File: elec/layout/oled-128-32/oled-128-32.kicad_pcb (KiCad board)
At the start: 2 copper layers, 1.5 x 10.5 mm, 14 parts

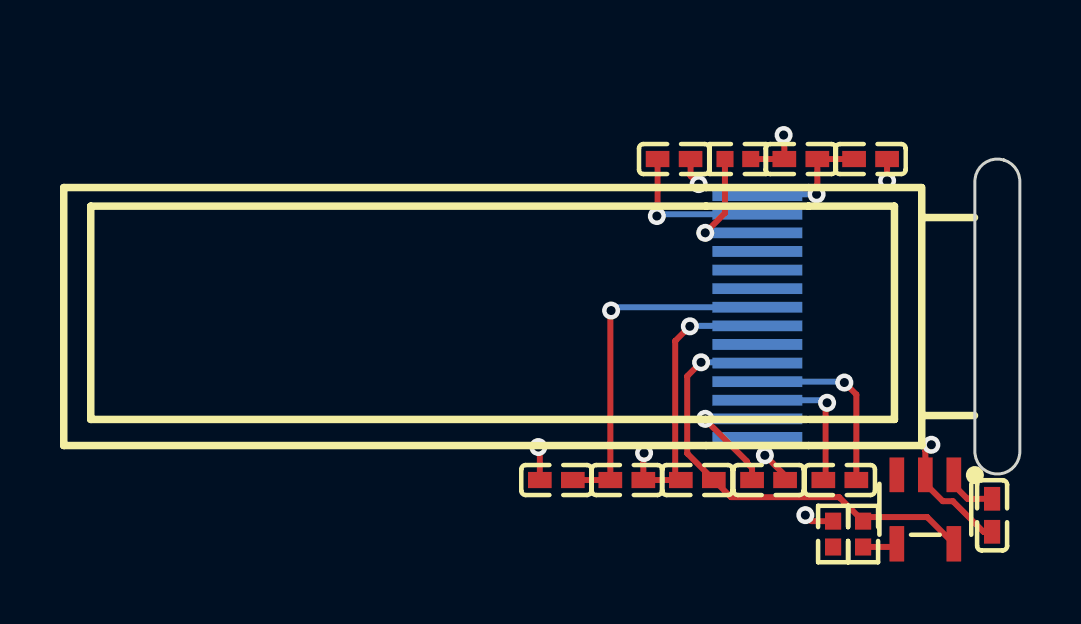
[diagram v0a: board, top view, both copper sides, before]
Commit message: cleanup CM5 pinout
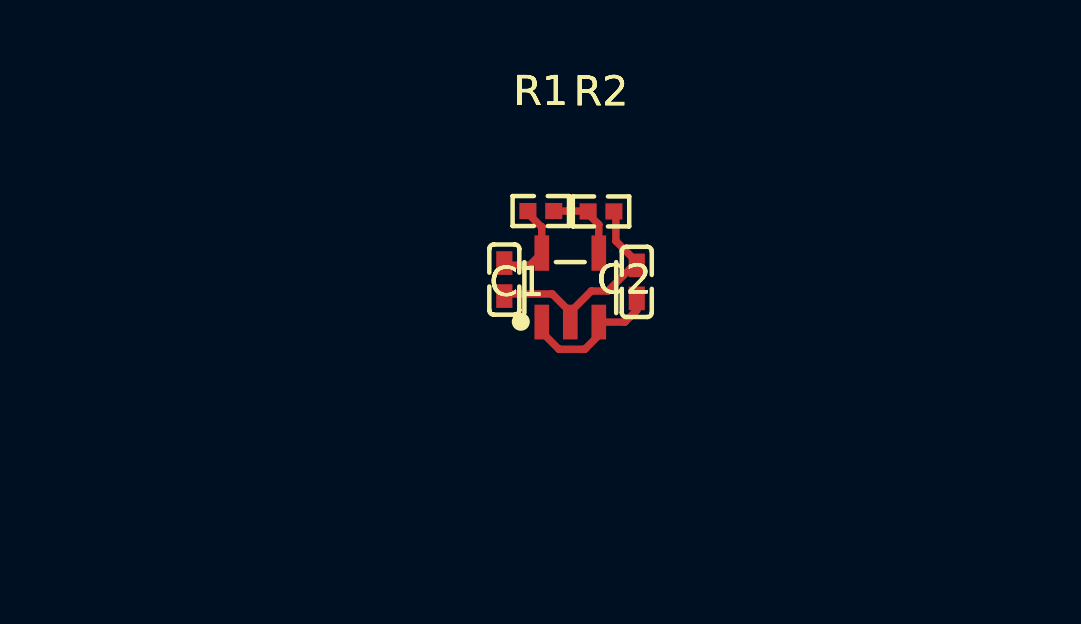
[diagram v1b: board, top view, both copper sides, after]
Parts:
- removed C3, C4: 1µF ±10% 25V X5R, atopile:C0402-b3ef17
- removed C5, C7, C8, C9: 100nF ±10% 16V X7R, atopile:C0402-b3ef17
- removed C6: 4.7µF ±20% 6.3V X5R, atopile:C0402-b3ef17
- removed OLED1: , atopile:OLED-SMD_N087-2832TSWYG02-H14_1-7d3a70
- removed R3: 10kΩ ±1% 62.5mW, atopile:R0402-56259e
- R1: value 510kΩ ±1% 62.5mW -> 18kΩ ±1% 62.5mW
- R2: value 3.9kΩ ±1% 62.5mW -> 10kΩ ±1% 62.5mW
- moved U1 14.0 mm to (148.6, 111.8), turned to 0 degrees
- moved R2 13.2 mm to (149.6, 109.2), turned to 0 degrees
- moved C2 11.1 mm to (146.4, 111.5), turned to -90 degrees
- moved C1 9.46 mm to (150.8, 111.6), turned to 90 degrees
- moved R1 6.79 mm to (147.6, 109.2)
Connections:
- C1 pad 1: C1N -> IN
- C1 pad 2: C1P -> gnd
- C2 pad 1: C2N -> OUT
- C2 pad 2: C2P -> gnd
- R1 pad 1: IREF -> OUT
- R1 pad 2: gnd -> ADJ_NC
- U1 pad 1: hv-1 -> IN
- U1 pad 3: hv-1 -> IN
- U1 pad 5: hv-3 -> OUT
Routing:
- net hv-3: track 15.4 -> 0.00 mm, vias 1 -> 0
- net gnd: track 19.8 -> 7.73 mm, vias 8 -> 0
- net hv-2: track 11.8 -> 0.00 mm, vias 1 -> 0
- net C1N: track 6.33 -> 0.00 mm, vias 1 -> 0
- net VCOMH: track 5.29 -> 0.00 mm, vias 1 -> 0
- net IN: track 0.00 -> 5.00 mm
- net C1P: track 4.99 -> 0.00 mm, vias 1 -> 0
- net IREF: track 4.47 -> 0.00 mm, vias 1 -> 0
- net C2N: track 4.42 -> 0.00 mm, vias 1 -> 0
- net hv: track 4.40 -> 0.00 mm, vias 1 -> 0
- net OUT: track 0.00 -> 3.05 mm
- net hv-1: track 1.81 -> 0.00 mm
- net C2P: track 1.80 -> 0.00 mm, vias 1 -> 0
- net ADJ_NC: track 1.17 -> 2.56 mm
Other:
- board outline removed

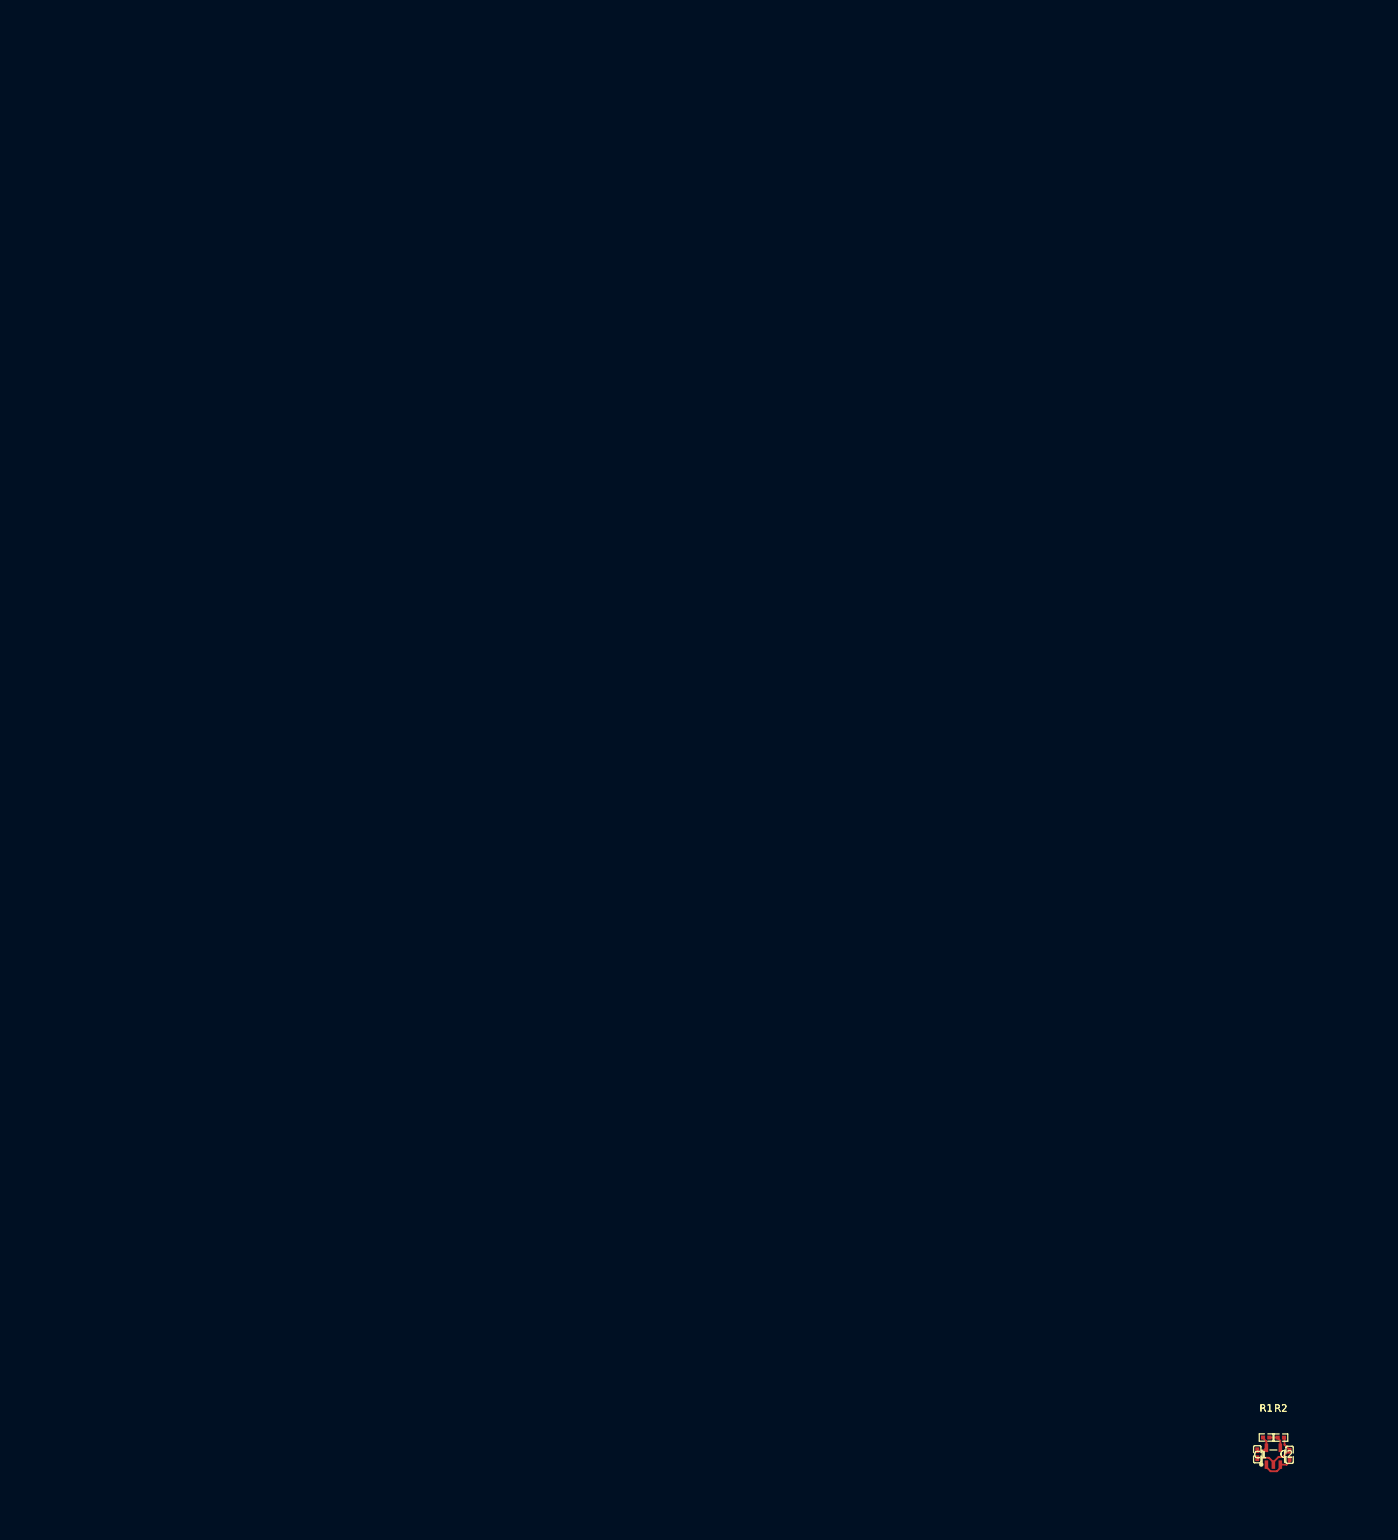
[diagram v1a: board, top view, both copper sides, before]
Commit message: update layouts to kicad 9
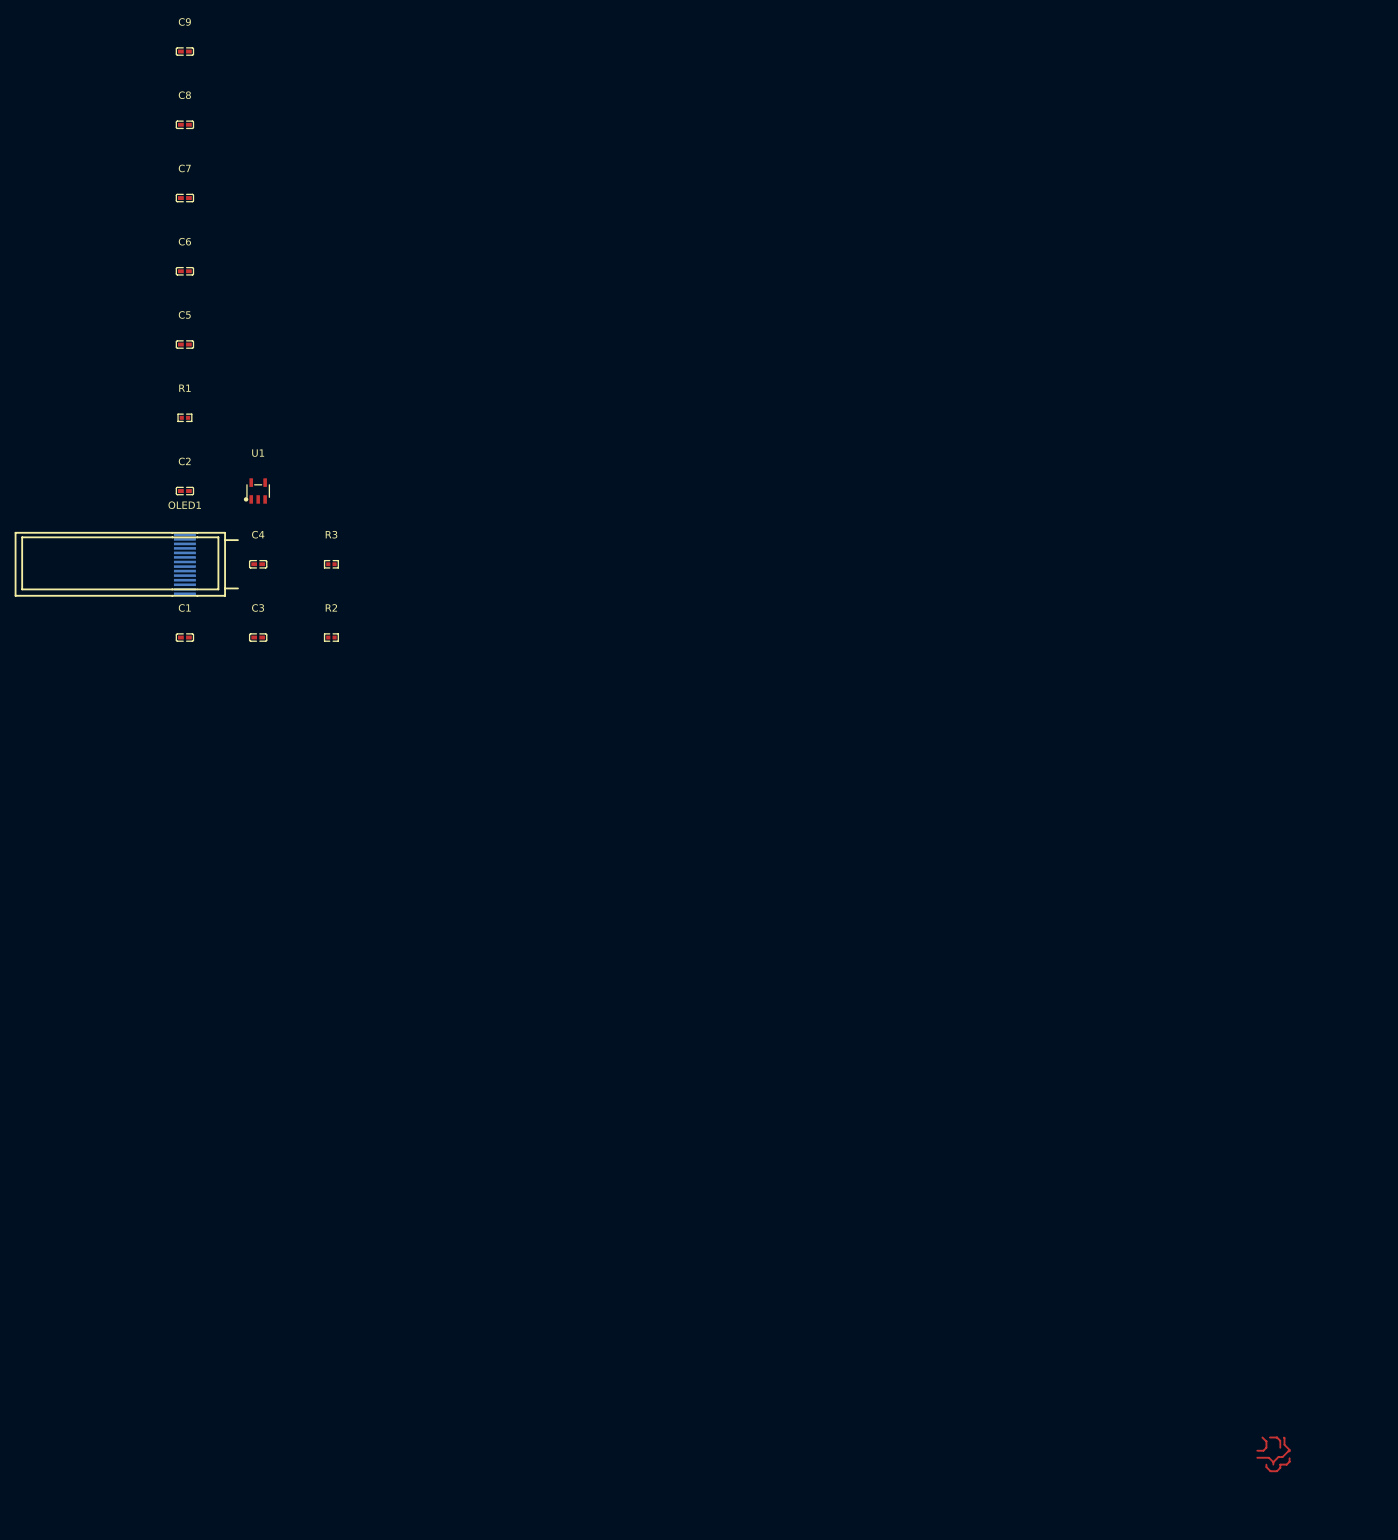
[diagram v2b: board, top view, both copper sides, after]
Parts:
- added C3: 1µF ±10% 25V X5R, atopile:C0402-b3ef17, F.Cu at (10.0, 0.00)
- added C4: 1µF ±10% 25V X5R, atopile:C0402-b3ef17, F.Cu at (10.0, -10.0)
- added C5: 100nF ±10% 16V X7R, atopile:C0402-b3ef17, F.Cu at (0.00, -40.0)
- added C6: 4.7µF ±20% 6.3V X5R, atopile:C0402-b3ef17, F.Cu at (0.00, -50.0)
- added C7: 100nF ±10% 16V X7R, atopile:C0402-b3ef17, F.Cu at (0.00, -60.0)
- added C8: 100nF ±10% 16V X7R, atopile:C0402-b3ef17, F.Cu at (0.00, -70.0)
- added C9: 100nF ±10% 16V X7R, atopile:C0402-b3ef17, F.Cu at (0.00, -80.0)
- added OLED1: , atopile:OLED-SMD_N087-2832TSWYG02-H14_1-7d3a70, F.Cu at (0.00, -10.0)
- added R3: 10kΩ ±1% 62.5mW, atopile:R0402-56259e, F.Cu at (20.0, -10.0)
- R1: value 18kΩ ±1% 62.5mW -> 510kΩ ±1% 62.5mW
- R2: value 10kΩ ±1% 62.5mW -> 3.9kΩ ±1% 62.5mW
- moved R1 202.9 mm to (0.00, -30.0)
- moved C2 196.8 mm to (0.00, -20.0), turned to 0 degrees
- moved U1 191.2 mm to (10.0, -20.0)
- moved C1 187.6 mm to (0.00, 0.00), turned to 0 degrees
- moved R2 169.5 mm to (20.0, 0.00)
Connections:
- C1 pad 1: IN -> C1N
- C1 pad 2: gnd -> C1P
- C2 pad 1: OUT -> C2N
- C2 pad 2: gnd -> C2P
- R1 pad 1: OUT -> IREF
- R1 pad 2: ADJ_NC -> gnd
- U1 pad 1: IN -> hv-1
- U1 pad 3: IN -> hv-1
- U1 pad 5: OUT -> hv
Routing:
- net (no net): track 0.00 -> 18.3 mm
- net gnd: track 7.73 -> 0.00 mm
- net IN: track 5.00 -> 0.00 mm
- net OUT: track 3.05 -> 0.00 mm
- net ADJ_NC: track 2.56 -> 0.00 mm

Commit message: building frozen
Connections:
- net line renamed SCL
- net line-1 renamed SDA
- C4 pad 1: hv -> hv-2
- C5 pad 1: hv-2 -> hv-3
- C6 pad 1: hv-2 -> hv-3
- C8 pad 1: hv-3 -> hv
- C9 pad 1: hv-3 -> hv
- OLED1 pad 14: hv-2 -> hv-3
- OLED1 pad 5: hv -> hv-2
- OLED1 pad 8: hv-3 -> hv
- R3 pad 1: hv -> hv-2
- U1 pad 5: hv -> hv-2

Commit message: Build everything with ordered params to fix frozen builds
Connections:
- C3 pad 1: hv-1 -> hv
- C4 pad 1: hv-2 -> hv-3
- C5 pad 1: hv-3 -> hv-2
- C6 pad 1: hv-3 -> hv-2
- C8 pad 1: hv -> hv-1
- C9 pad 1: hv -> hv-1
- OLED1 pad 14: hv-3 -> hv-2
- OLED1 pad 5: hv-2 -> hv-3
- OLED1 pad 8: hv -> hv-1
- R3 pad 1: hv-2 -> hv-3
- U1 pad 1: hv-1 -> hv
- U1 pad 3: hv-1 -> hv
- U1 pad 5: hv-2 -> hv-3
